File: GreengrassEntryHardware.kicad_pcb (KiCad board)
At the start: 2 copper layers, 66 x 57 mm, 31 parts, among them J1 USB_B_Micro, J2 GPIOBreakout, J3 Raspberry_Pi_2_3, J4 AutomaticSlidingDoor, J5 MFRC-522, U1 CH340G, Y1 12MHZ

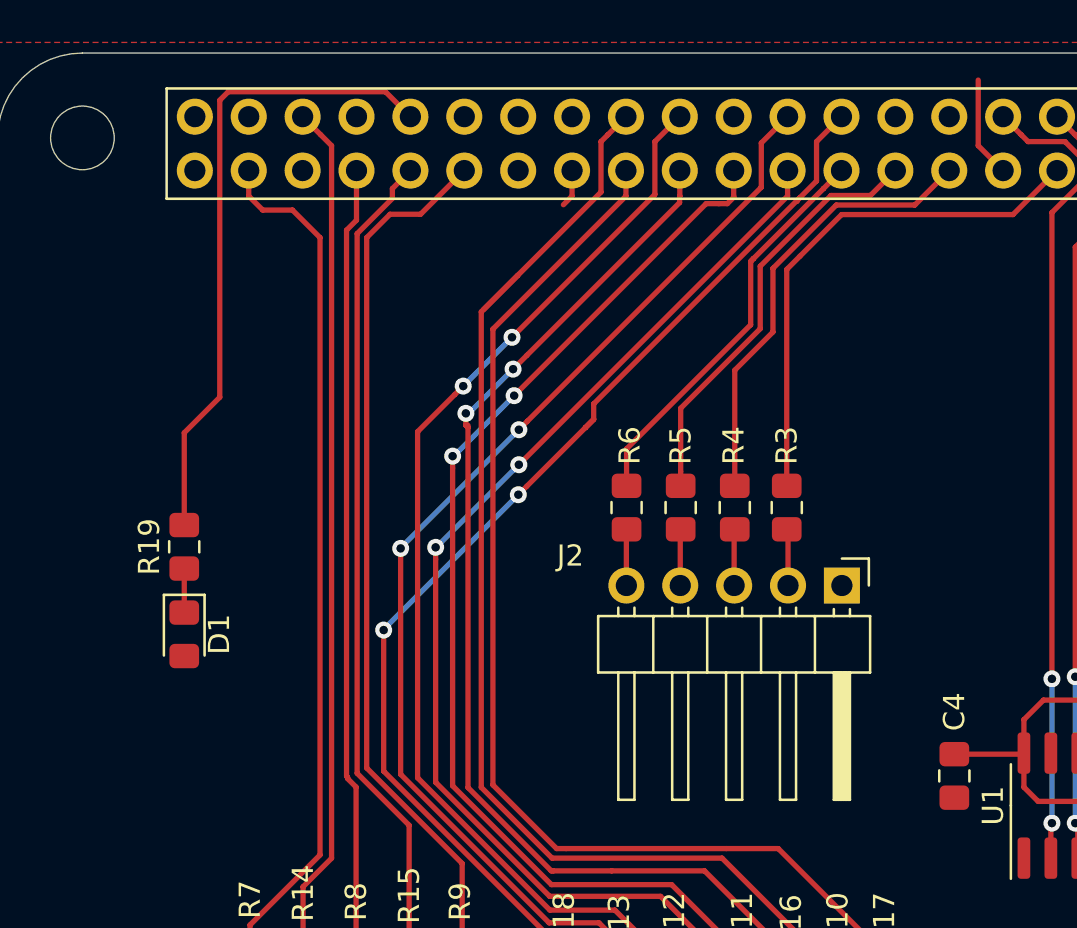
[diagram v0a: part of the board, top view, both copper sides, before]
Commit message: Some tweaks before changing mfrc connector to molex
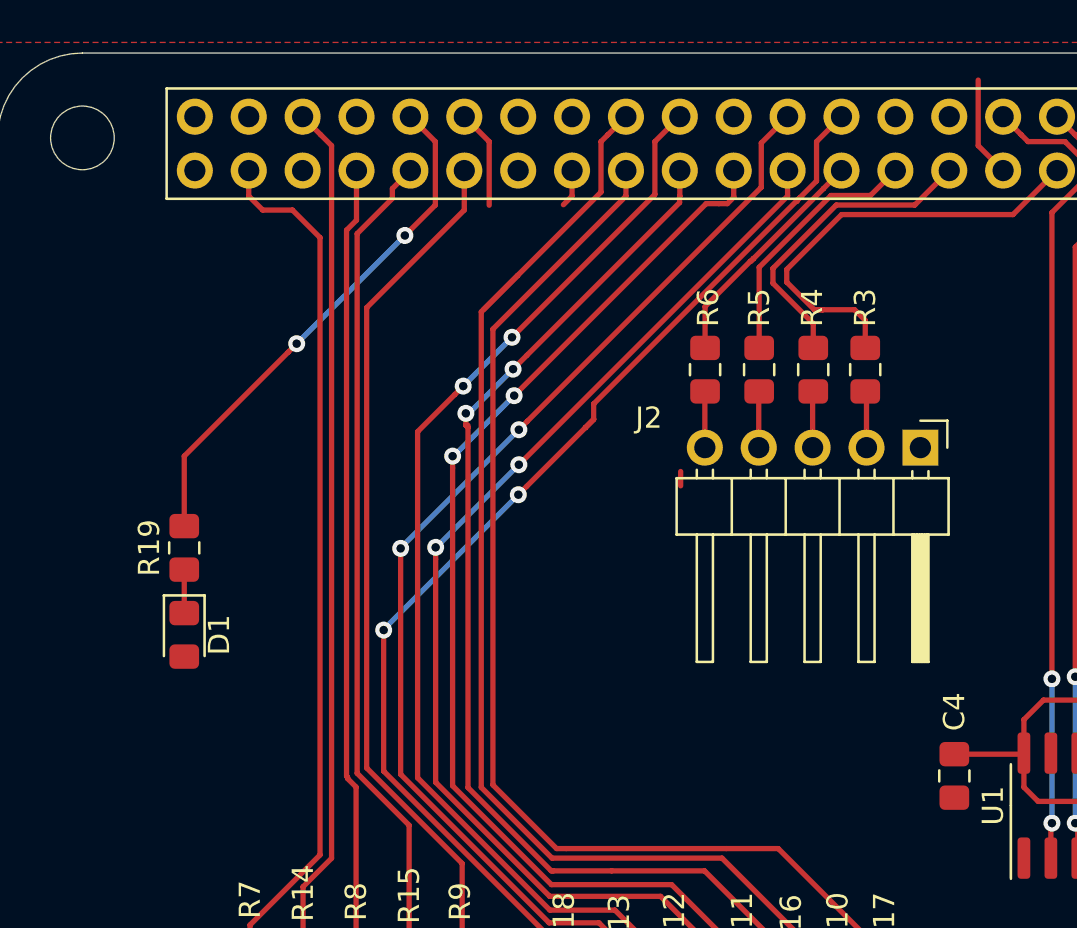
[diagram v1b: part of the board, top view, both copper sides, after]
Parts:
- moved R3 7.48 mm to (224.9, 65.9)
- moved R5 7.48 mm to (219.9, 65.9)
- moved J2 7.48 mm to (227.5, 69.6)
- moved R4 7.48 mm to (222.4, 65.9)
- moved R6 7.48 mm to (217.3, 65.9)
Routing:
- net Net-(J3-Pad15): track 19.2 -> 11.2 mm
- net Net-(J3-Pad13): track 20.1 -> 12.8 mm
- net Net-(J3-Pad11): track 21.2 -> 14.8 mm
- net Net-(J3-Pad32): track 30.4 -> 24.6 mm, vias 0 -> 2
- net GNDD: track 6.53 -> 11.2 mm
- net Net-(J3-Pad7): track 24.9 -> 21.3 mm
- net Net-(J3-Pad29): track 41.1 -> 40.3 mm

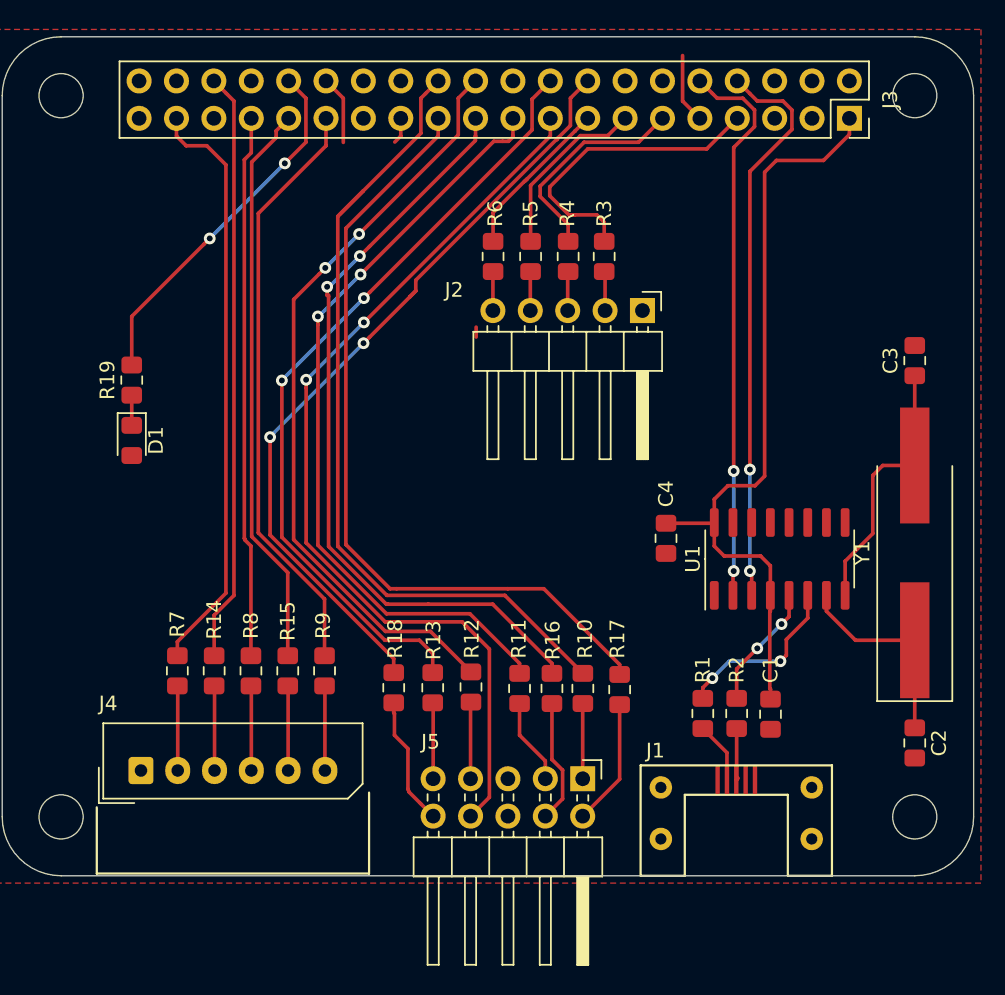
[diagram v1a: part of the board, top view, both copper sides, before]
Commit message: Added molex connector for mfrc and added net labels
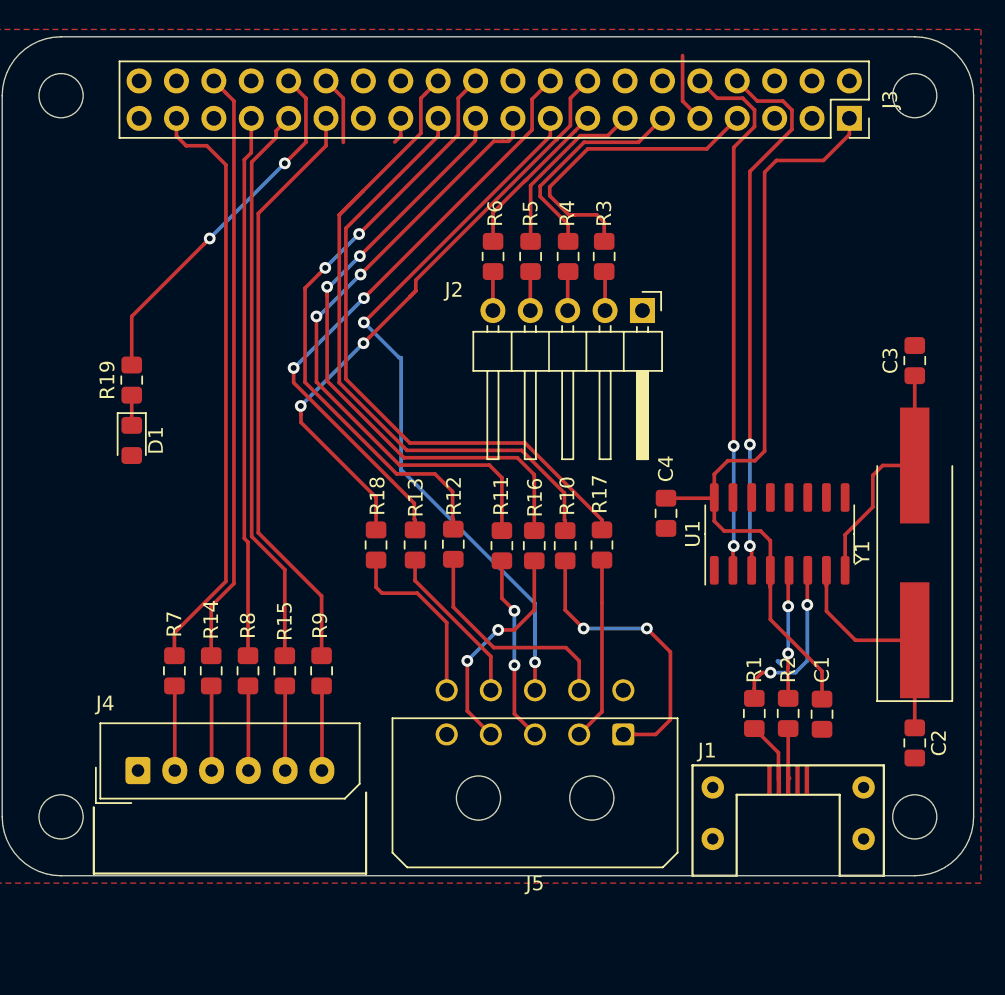
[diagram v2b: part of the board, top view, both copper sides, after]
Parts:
- J5: footprint Connector_PinHeader_2.54mm:PinHeader_2x05_P2.54mm_Horizontal -> GreengrassEntryHardware:Molex_Micro-Fit_3.0_43045-1000_2x05_P3.00mm_Horizontal
- moved R17 9.90 mm to (224.8, 85.5)
- moved R11 9.77 mm to (217.9, 85.6)
- moved R10 9.77 mm to (222.2, 85.6)
- moved R12 9.77 mm to (214.7, 85.5)
- moved R16 9.77 mm to (220.2, 85.6)
- moved R13 9.77 mm to (212.1, 85.5)
- moved R18 9.77 mm to (209.4, 85.5)
- moved J5 4.08 mm to (226.2, 98.4), turned to 180 degrees
- moved J1 3.53 mm to (237.4, 102.5)
- moved C1 3.50 mm to (239.7, 97.0)
- moved R1 3.50 mm to (235.1, 97.0)
- moved R2 3.50 mm to (237.4, 97.0)
- moved C4 1.70 mm to (229.1, 83.4)
- moved U1 1.70 mm to (236.8, 84.8)
- moved J4 0.20 mm to (193.2, 100.8)
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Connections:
- net Net-(J1-Pad2) renamed /D-
- net Net-(J1-Pad3) renamed /D+
- net Net-(J2-Pad2) renamed /GPIO4
- net Net-(J2-Pad3) renamed /GPIO17
- net Net-(J2-Pad4) renamed /GPIO27
- net Net-(J2-Pad5) renamed /GPIO22
- net Net-(J3-Pad17) renamed /3.3V
- net Net-(J4-Pad2) renamed /EXIT
- net Net-(J4-Pad3) renamed /OPEN
- net Net-(J4-Pad4) renamed /AUTO
- net Net-(J4-Pad5) renamed /AUTO_OUT
- net Net-(J4-Pad6) renamed /CLOSED
- net Net-(J5-Pad1) renamed /SDA-CS
- net Net-(J5-Pad10) renamed /BUZZER
- net Net-(J5-Pad2) renamed /SCK
- net Net-(J5-Pad3) renamed /MOSI
- net Net-(J5-Pad4) renamed /MISO
- net Net-(J5-Pad7) renamed /RST
- net Net-(J5-Pad9) renamed /LED
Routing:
- net /SDA-CS: track 5.11 -> 19.9 mm, vias 0 -> 2
- net /3.3V: track 63.6 -> 49.6 mm
- net Net-(J3-Pad18): track 53.4 -> 41.2 mm
- net Net-(J3-Pad16): track 53.4 -> 41.4 mm
- net Net-(J3-Pad23): track 54.2 -> 42.3 mm
- net Net-(J3-Pad22): track 52.1 -> 40.9 mm
- net Net-(J3-Pad24): track 57.0 -> 46.6 mm
- net /RST: track 5.22 -> 15.3 mm
- net Net-(J3-Pad19): track 52.8 -> 43.1 mm
- net Net-(J3-Pad21): track 52.6 -> 43.2 mm
- net /MOSI: track 5.83 -> 12.7 mm, vias 0 -> 2
- net /MISO: track 8.44 -> 15.0 mm, vias 0 -> 2
- net /LED: track 5.17 -> 11.0 mm
- net /SCK: track 8.61 -> 12.5 mm
- net /BUZZER: track 8.79 -> 12.2 mm
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
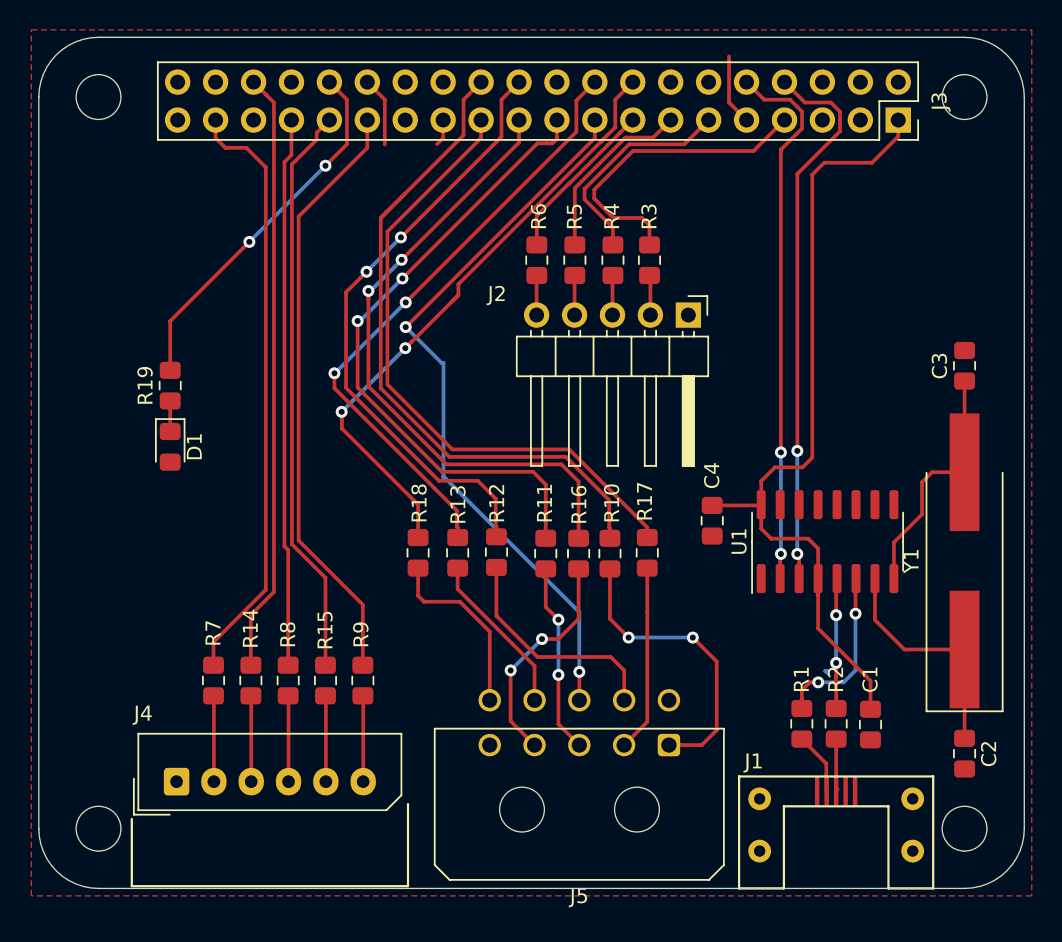
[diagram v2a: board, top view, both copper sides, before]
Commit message: Increase vias size, design rules, back plane, copyright
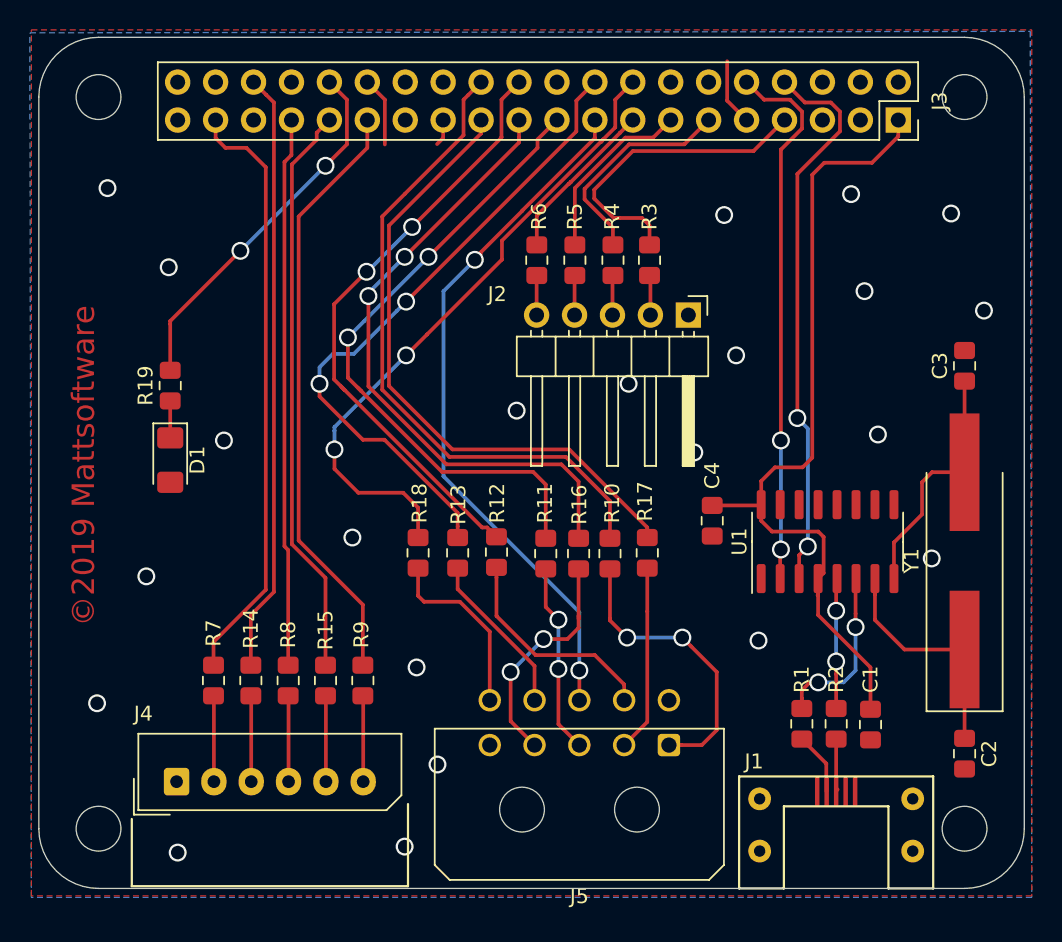
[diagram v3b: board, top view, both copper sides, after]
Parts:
- D1: footprint LED_SMD:LED_0805_2012Metric_Pad1.15x1.40mm_HandSolder -> LED_SMD:LED_1206_3216Metric_Pad1.42x1.75mm_HandSolder
- moved D1 0.89 mm to (192.8, 79.3)
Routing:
- net /3.3V: track 49.6 -> 46.8 mm
- net Net-(J3-Pad18): track 41.2 -> 43.6 mm
- net Net-(J3-Pad24): track 46.6 -> 44.2 mm
- net Net-(J3-Pad16): track 41.4 -> 43.0 mm
- net Net-(J3-Pad8): track 37.0 -> 37.7 mm
- net Net-(C1-Pad1): track 55.1 -> 55.7 mm
- net /RST: track 15.3 -> 14.8 mm
- net GNDD: track 11.2 -> 10.9 mm, vias 0 -> 22
- added copper zone on B.Cu, net GNDD
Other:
- net class Default: via_dia 0.8 -> 1.2; via_drill 0.4 -> 0.9
- rule via_min_drill: 0.3 -> 0.9
- rule via_min_size: 0.4 -> 1.2
- board text added: "©2019 Mattsoftware"

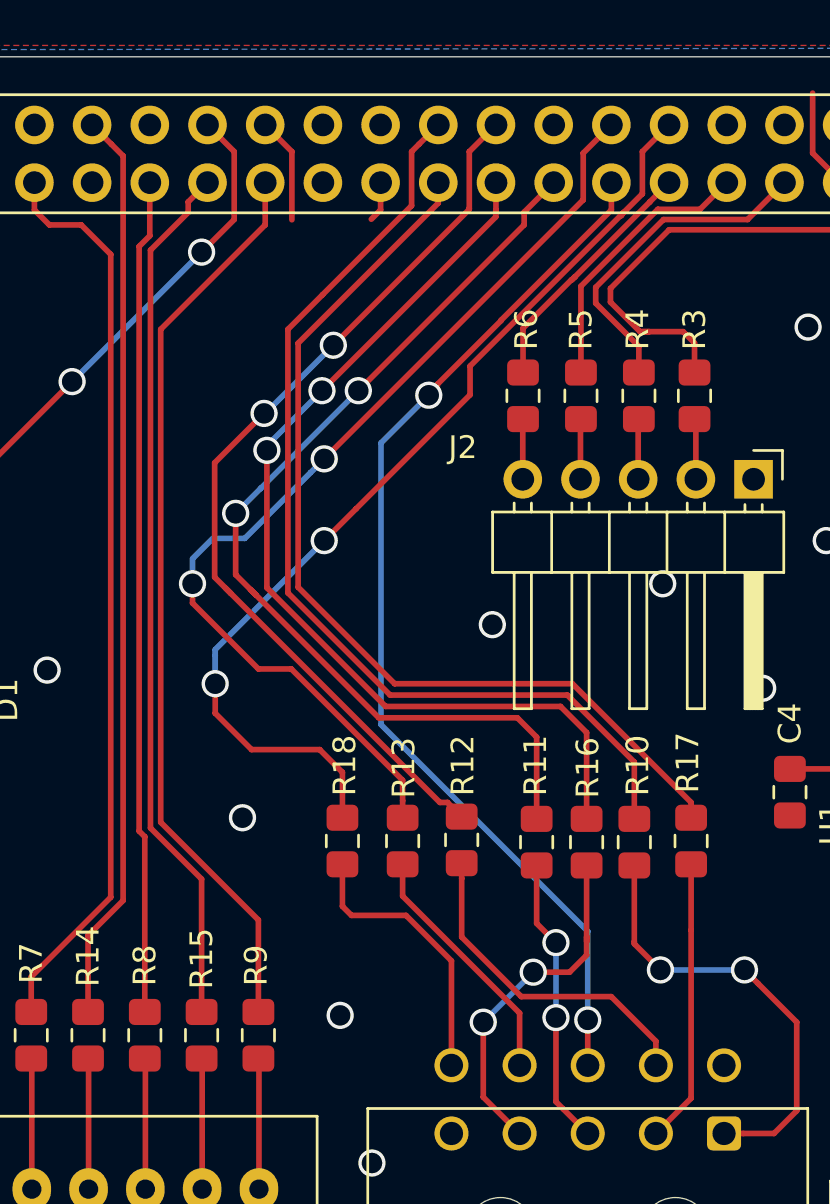
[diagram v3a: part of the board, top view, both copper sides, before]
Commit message: Tweak some tracks to maximise groundplane
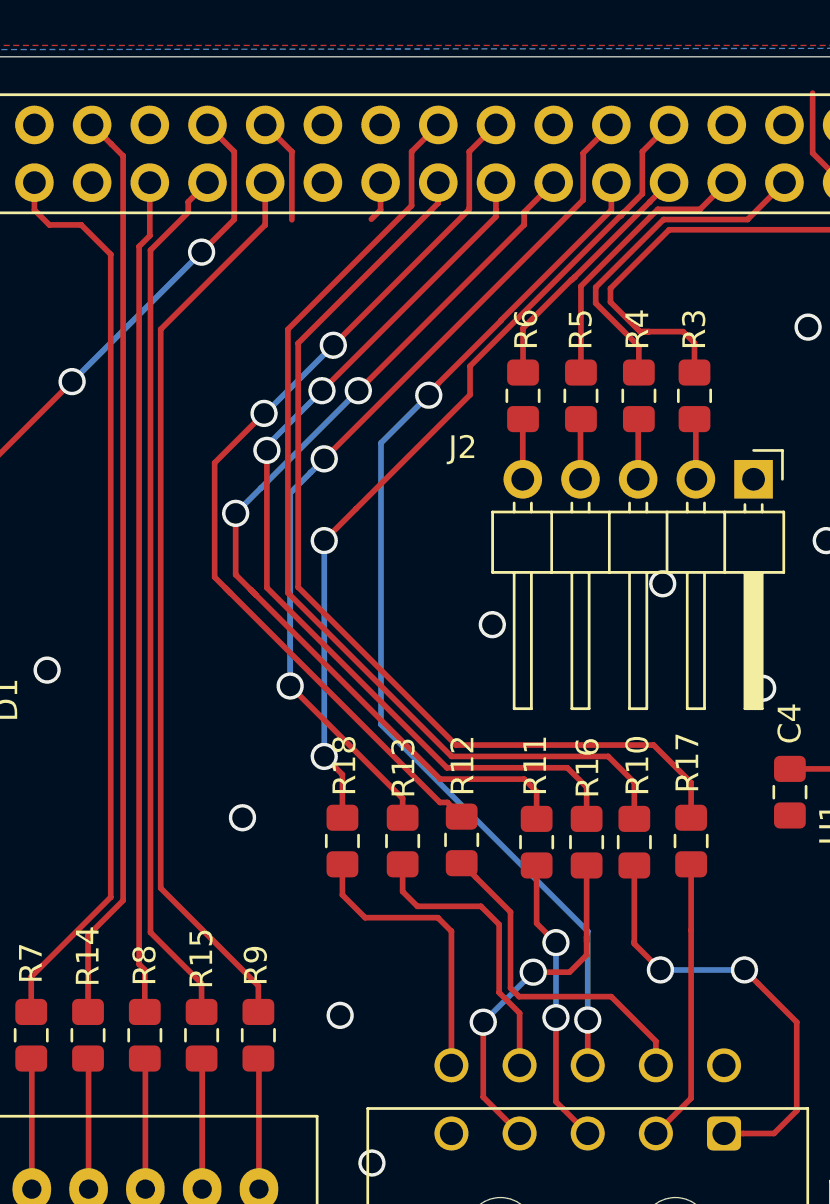
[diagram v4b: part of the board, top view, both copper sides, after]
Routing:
- net Net-(J3-Pad16): track 43.0 -> 37.3 mm
- net Net-(J3-Pad18): track 43.6 -> 38.4 mm
- net Net-(J3-Pad21): track 43.4 -> 41.4 mm
- net /LED: track 11.0 -> 12.6 mm
- net Net-(J3-Pad19): track 43.2 -> 41.8 mm
- net Net-(J3-Pad24): track 44.2 -> 43.7 mm
- net Net-(J3-Pad23): track 42.3 -> 42.8 mm
